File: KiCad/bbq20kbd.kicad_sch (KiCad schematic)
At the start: 23 parts, among them Q3 BSS138, Q4 BSS138, Q5 BSS138, Q6 BSS138, Q7 BSS138, Q8 BSS138, U7 ME6212C18M5G, U8 ME6212C28M5G, U9 BBQ20KBD

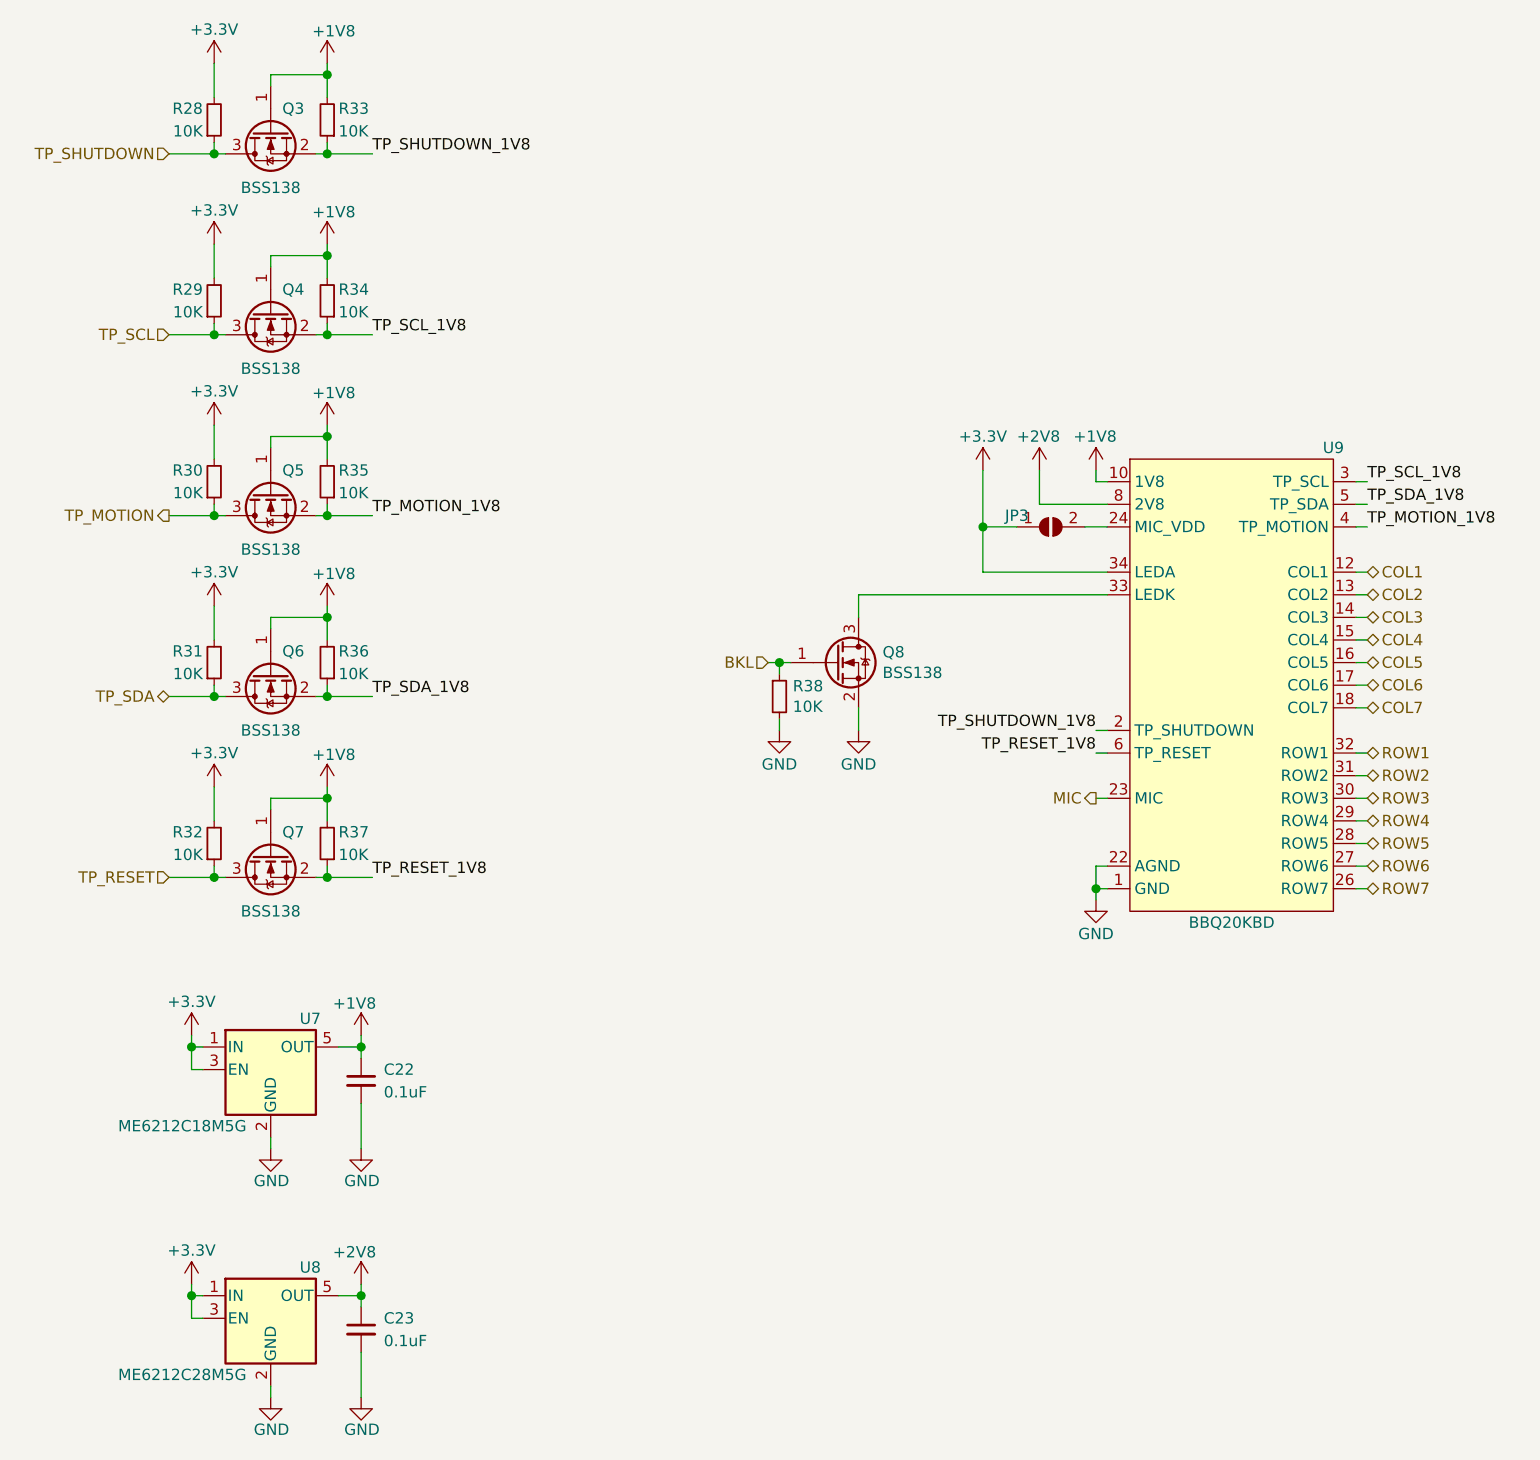
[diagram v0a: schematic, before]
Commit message: Moved 4 layers to 2 layers with ground fill
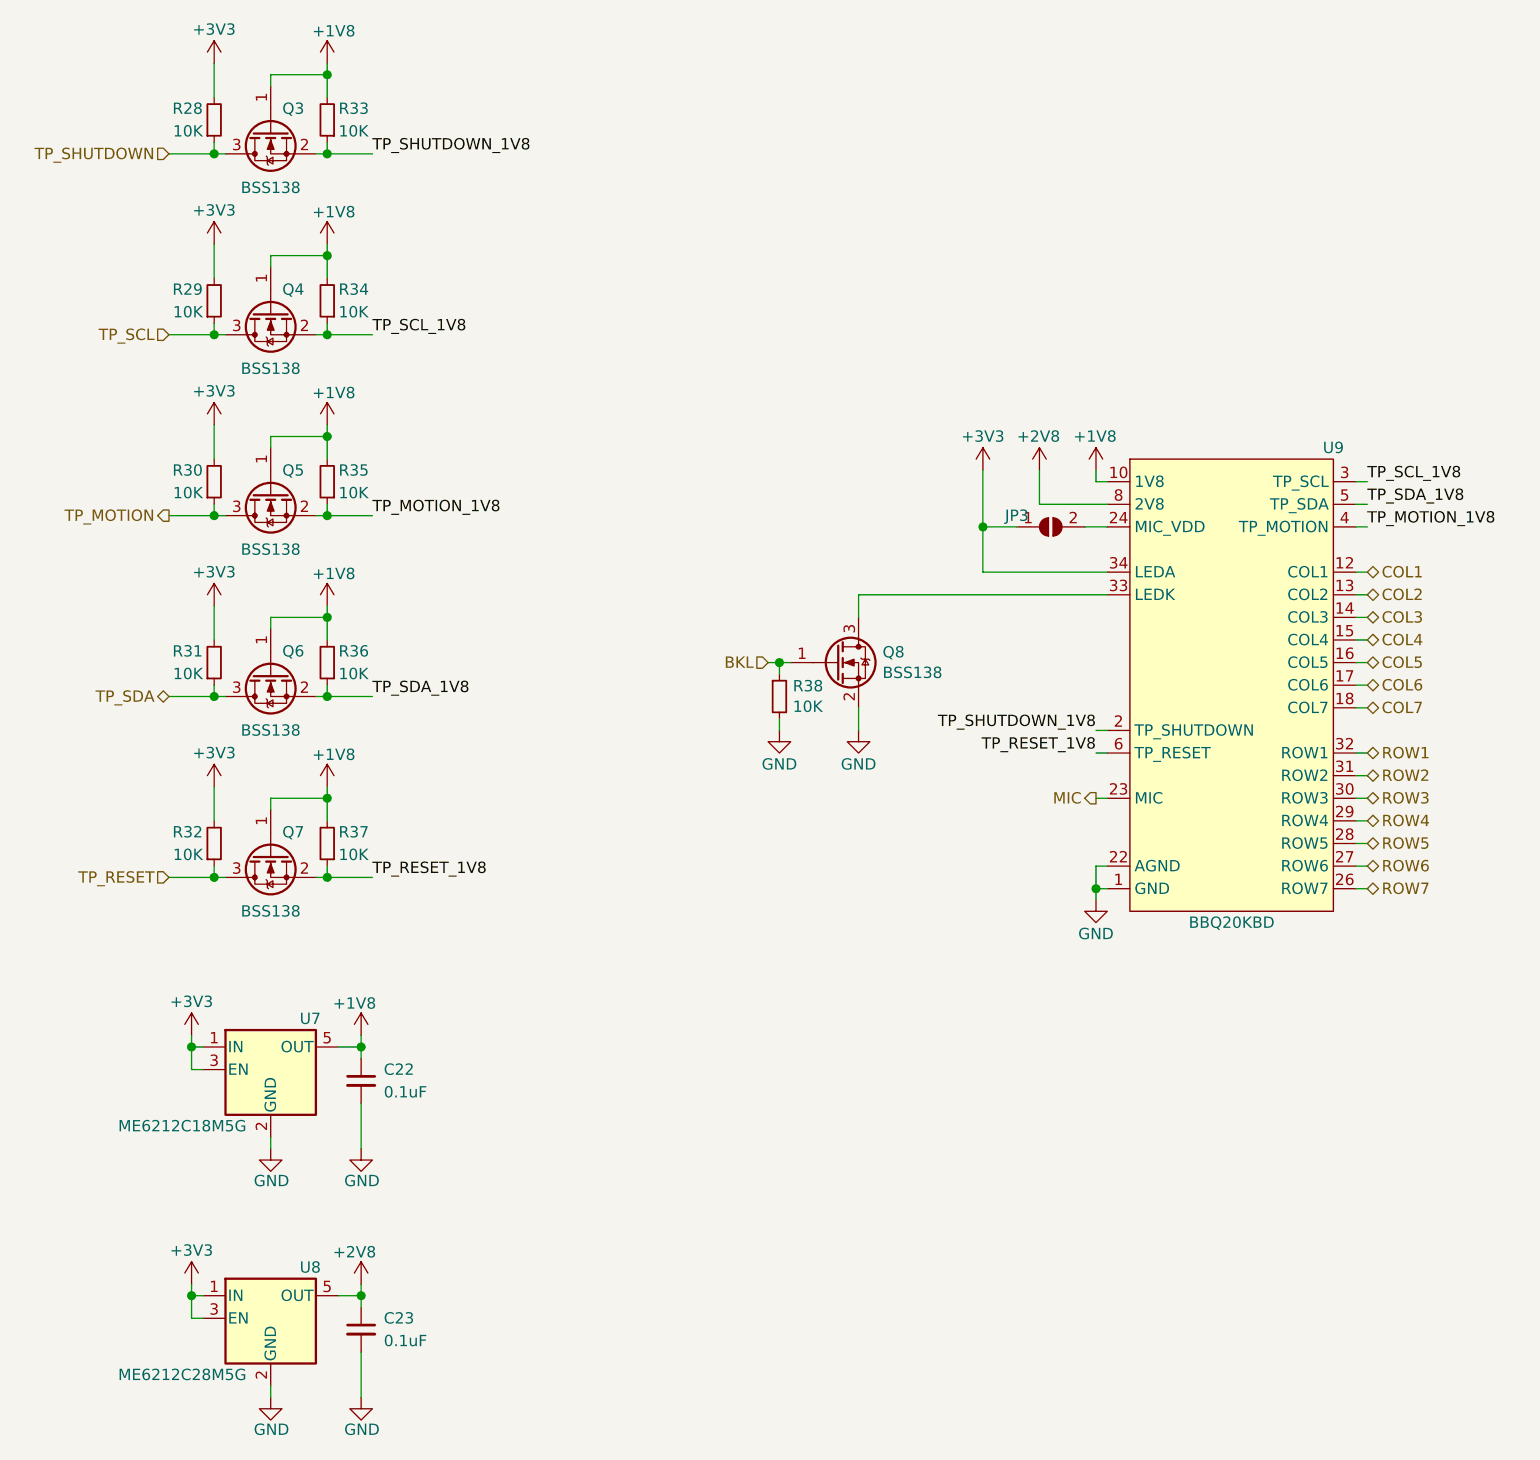
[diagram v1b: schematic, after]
